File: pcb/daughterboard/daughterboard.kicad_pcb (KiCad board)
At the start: 2 copper layers, 82.5 x 25.4 mm, 0 parts

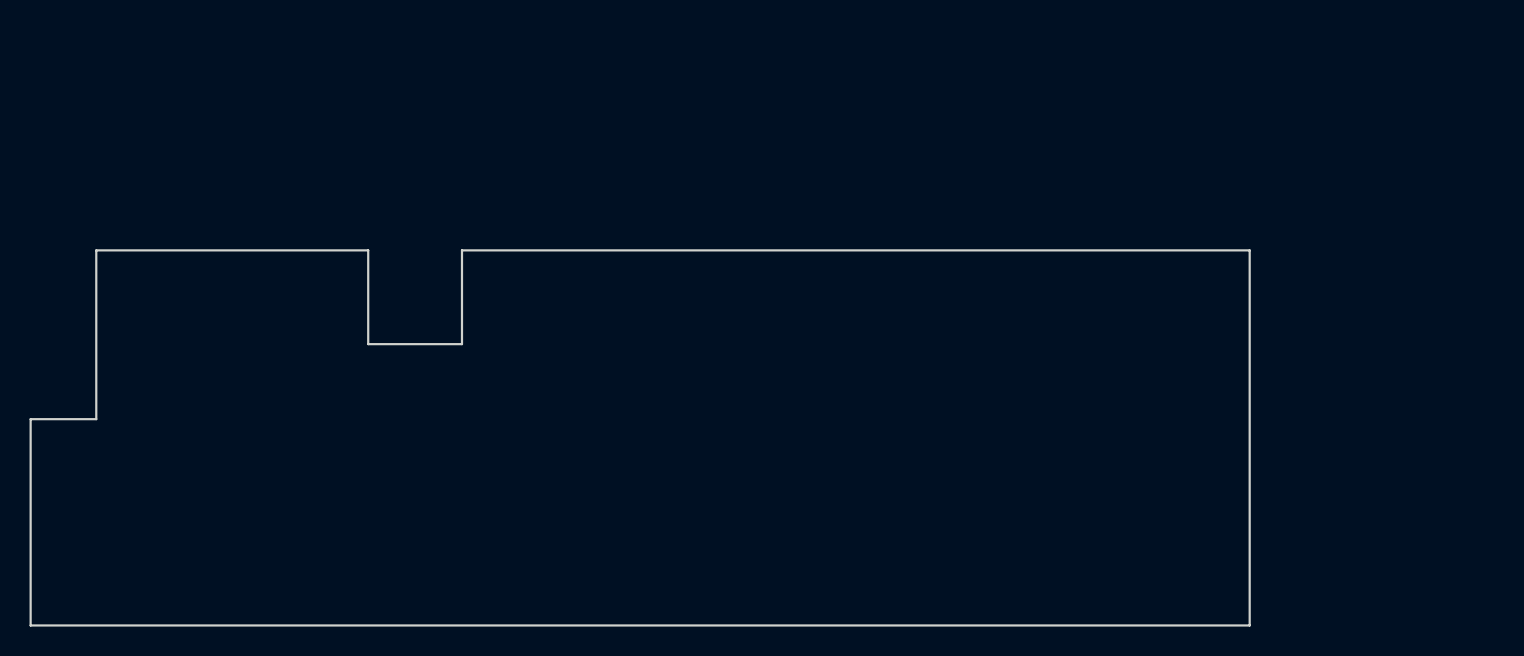
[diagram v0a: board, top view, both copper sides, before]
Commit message: Modified daughterboard board layout
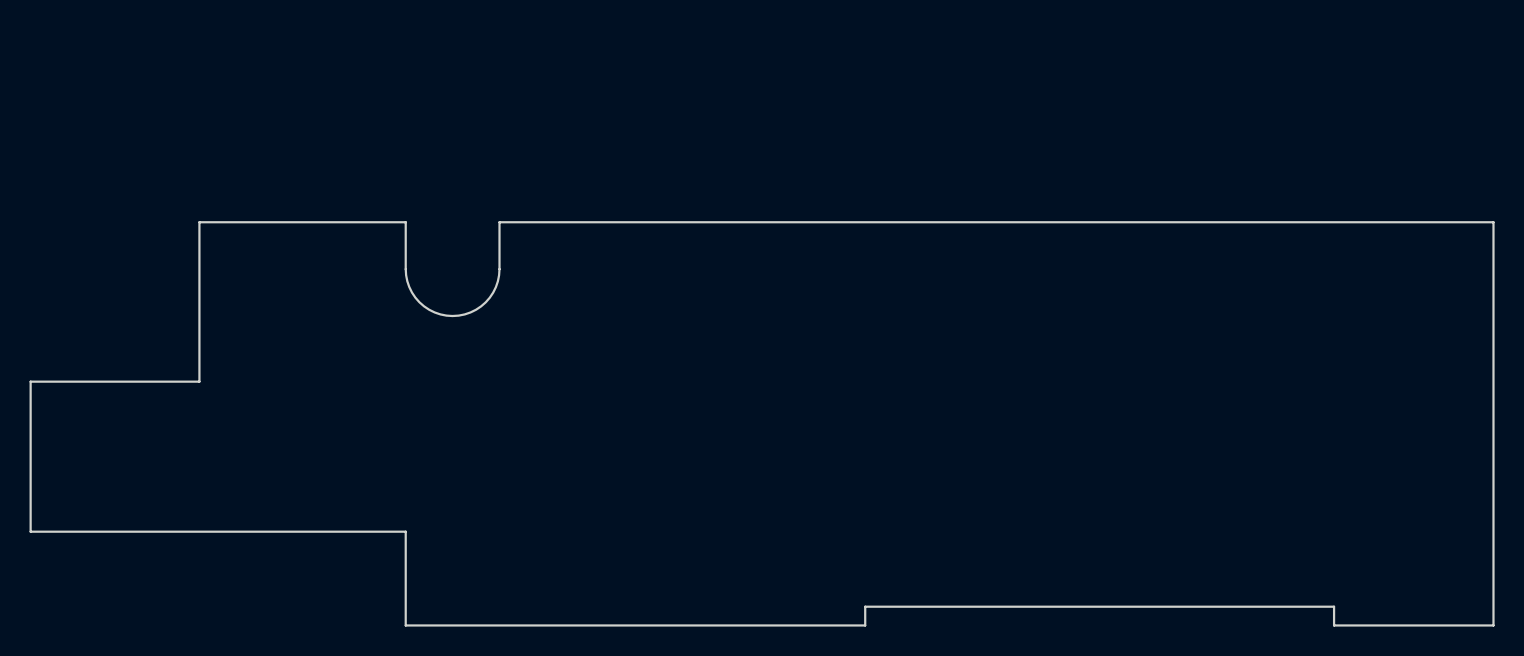
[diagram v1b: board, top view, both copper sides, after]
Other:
- board size 82.5 x 25.4 mm -> 99.1 x 27.3 mm
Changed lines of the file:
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@@
-(kicad_pcb (version 4) (host pcbnew "(2016-03-01 BZR 6238)-product")
+(kicad_pcb (version 4) (host pcbnew "(2016-05-03 BZR 6266)-product")
   (general
-    (links 3)
-    (no_connects 3)
-    (area 120.574999 87.18 177.875001 114.375001)
+    (links 0)
+    (no_connects 0)
+    (area 120.574999 86.919999 219.785001 114.375001)
     (thickness 1.6)
-    (drawings 10)
+    (drawings 16)
     (tracks 0)
     (zones 0)
@@
     (uvia_dia 0.3)
     (uvia_drill 0.1)
-    (add_net "Net-(J1-Pad1)")
-    (add_net "Net-(J1-Pad2)")
-    (add_net "Net-(J1-Pad3)")
-    (add_net "Net-(J1-Pad4)")
-    (add_net "Net-(J1-Pad5)")
-    (add_net "Net-(J1-Pad6)")
-    (add_net "Net-(J1-Pad7)")
-    (add_net "Net-(J1-Pad8)")
-    (add_net "Net-(J1-PadDC)")
-    (add_net "Net-(J1-PadDT)")
-    (add_net "Net-(J1-PadSH)")
   )
-  (gr_line (start 203.2 114.3) (end 120.65 114.3) (layer Edge.Cuts) (width 0.15))
-  (gr_line (start 203.2 88.9) (end 203.2 114.3) (layer Edge.Cuts) (width 0.15))
-  (gr_line (start 149.86 88.9) (end 203.2 88.9) (layer Edge.Cuts) (width 0.15))
-  (gr_line (start 149.86 95.25) (end 149.86 88.9) (layer Edge.Cuts) (width 0.15))
-  (gr_line (start 143.51 95.25) (end 149.86 95.25) (layer Edge.Cuts) (width 0.15))
-  (gr_line (start 143.51 88.9) (end 143.51 95.25) (layer Edge.Cuts) (width 0.15))
-  (gr_line (start 125.095 88.9) (end 143.51 88.9) (layer Edge.Cuts) (width 0.15))
-  (gr_line (start 125.095 100.33) (end 125.095 88.9) (layer Edge.Cuts) (width 0.15))
-  (gr_line (start 120.65 100.33) (end 125.095 100.33) (layer Edge.Cuts) (width 0.15))
-  (gr_line (start 120.65 114.3) (end 120.65 100.33) (layer Edge.Cuts) (width 0.15))
+  (gr_arc (start 149.225 90.17) (end 152.4 90.17) (angle 180) (layer Edge.Cuts) (width 0.15))
+  (gr_line (start 152.4 86.995) (end 152.4 90.17) (layer Edge.Cuts) (width 0.15))
+  (gr_line (start 146.05 86.995) (end 146.05 90.17) (layer Edge.Cuts) (width 0.15))
+  (gr_line (start 152.4 86.995) (end 219.71 86.995) (layer Edge.Cuts) (width 0.15))
+  (gr_line (start 132.08 86.995) (end 146.05 86.995) (layer Edge.Cuts) (width 0.15))
+  (gr_line (start 132.08 97.79) (end 132.08 86.995) (layer Edge.Cuts) (width 0.15))
+  (gr_line (start 120.65 97.79) (end 132.08 97.79) (layer Edge.Cuts) (width 0.15))
+  (gr_line (start 120.65 107.95) (end 120.65 97.79) (layer Edge.Cuts) (width 0.15))
+  (gr_line (start 219.71 114.3) (end 219.71 86.995) (layer Edge.Cuts) (width 0.15))
+  (gr_line (start 208.915 114.3) (end 219.71 114.3) (layer Edge.Cuts) (width 0.15))
+  (gr_line (start 208.915 113.03) (end 208.915 114.3) (layer Edge.Cuts) (width 0.15))
+  (gr_line (start 177.165 113.03) (end 208.915 113.03) (layer Edge.Cuts) (width 0.15))
+  (gr_line (start 177.165 114.3) (end 177.165 113.03) (layer Edge.Cuts) (width 0.15))
+  (gr_line (start 146.05 114.3) (end 177.165 114.3) (layer Edge.Cuts) (width 0.15))
+  (gr_line (start 146.05 107.95) (end 146.05 114.3) (layer Edge.Cuts) (width 0.15))
+  (gr_line (start 120.65 107.95) (end 146.05 107.95) (layer Edge.Cuts) (width 0.15))
 )

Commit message: Revised touch and front panel PCB, Added Motherboard PCB
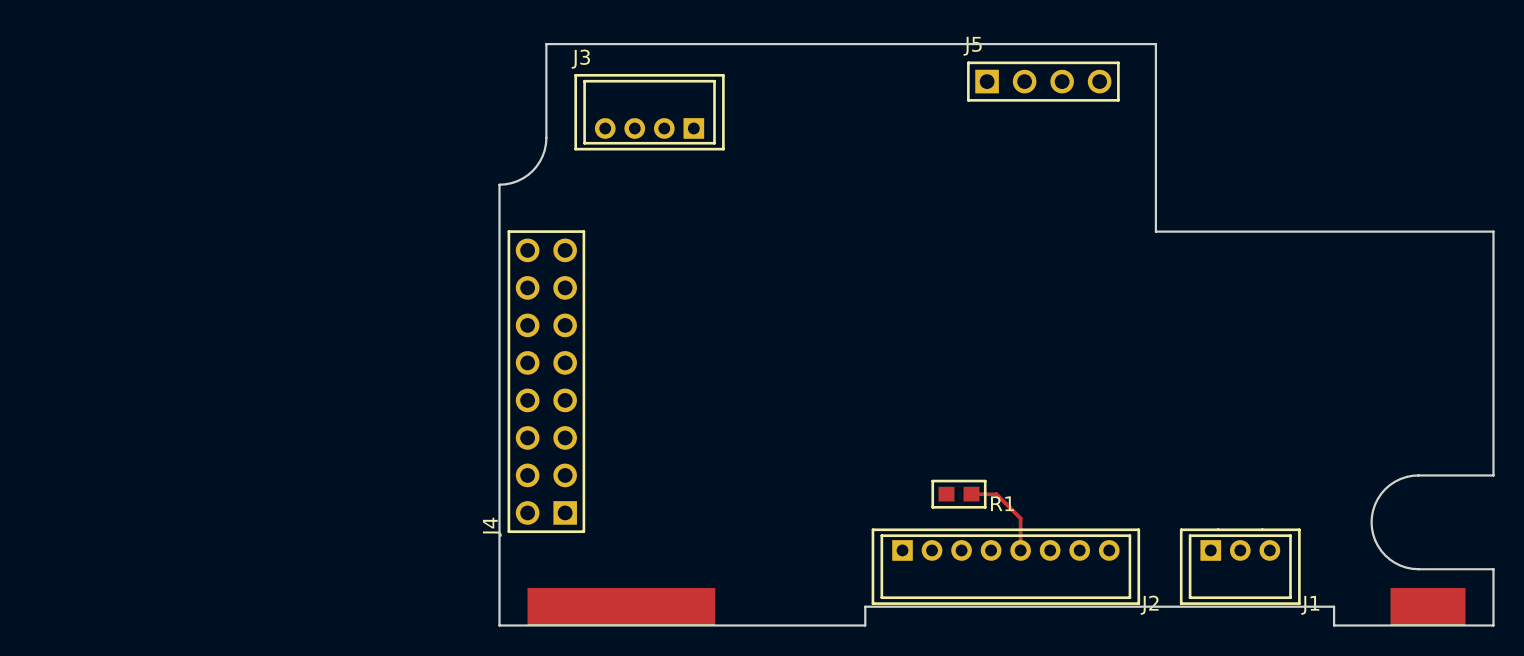
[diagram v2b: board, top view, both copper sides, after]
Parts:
- added H1: HEADER-1x01, conn-wire-pads:SolderPad-100x500, F.Cu at (160.7, 113.0)
- added H2: HEADER-1x01, conn-wire-pads:SolderPad-100x200, F.Cu at (215.3, 113.0)
- added J1: LAMP, conn-header:DF3A-3P-2DSA, F.Cu at (202.6, 109.2)
- added J2: DISPLAY, conn-header:DF3A-8P-2DSA, F.Cu at (186.7, 109.2)
- added J3: SPKR, conn-header:DF3A-4P-2DSA, F.Cu at (162.6, 80.6)
- added J4: MB I/O, conn-header:HDR-M-2x08, F.Cu at (155.6, 97.8)
- added J5: PWR, conn-header:HDR-M-1x04, F.Cu at (189.2, 77.5)
- added R1: 300, smt:R-0603, F.Cu at (183.5, 105.4)
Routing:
- net Net-(J2-Pad5): track 0.00 -> 6.18 mm
- added copper zone on POWER, net +5V
- added copper zone on GND, net GND
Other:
- board size 99.1 x 27.3 mm -> 67.3 x 39.4 mm
- copper layers 2 -> 4

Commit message: Updated PCB design
+ Completed daughterboard PCB layout.
* Corrected soldermask clerance on front panel pcb.
- Removed input resistor on DIN for RGB lamp board.
* Modified PCB layout for PSU board.
* Updated gerber files.
* Updated schematics pdf, BOM.
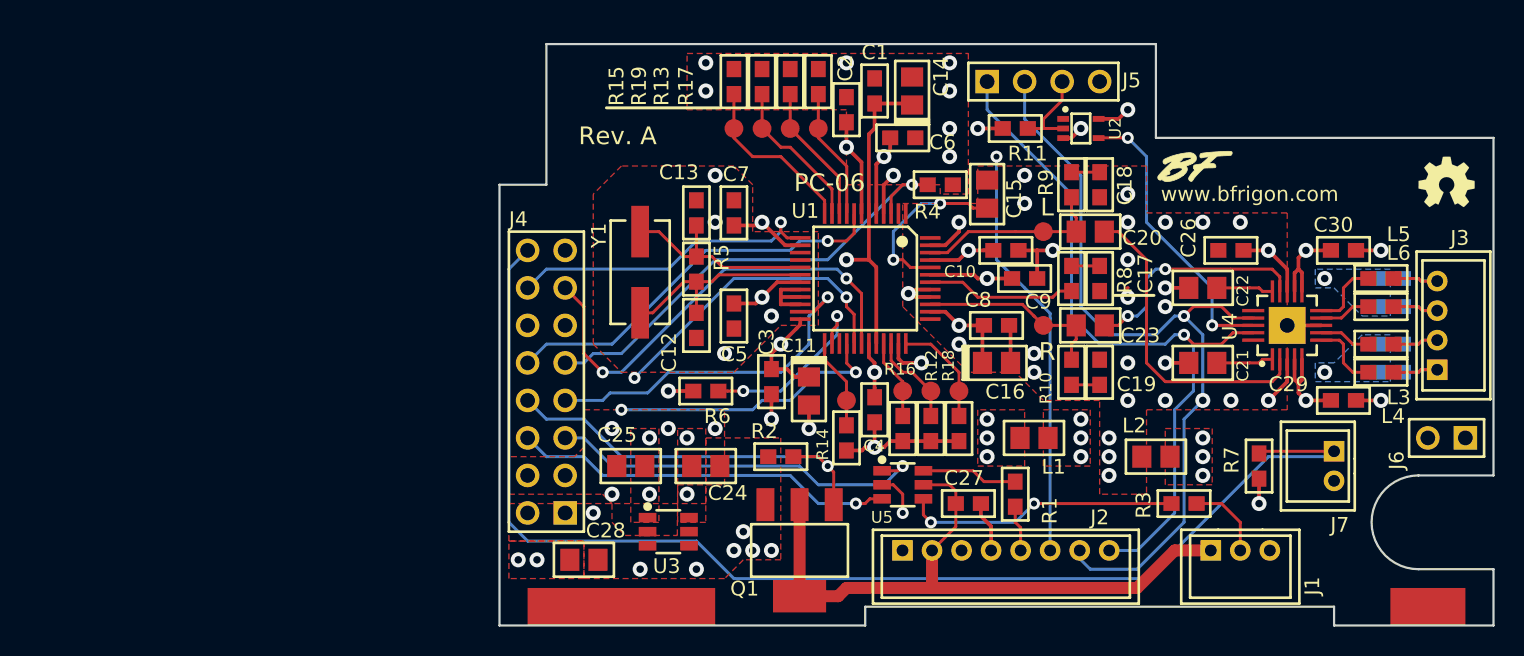
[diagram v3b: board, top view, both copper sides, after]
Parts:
- added C1: 100nF, smt:C-0603, F.Cu at (177.8, 78.1)
- added C10: 100nF, smt:C-0603, F.Cu at (186.7, 88.9)
- added C11: 10uF 6V3, smt:CPL-0805, F.Cu at (173.4, 98.4)
- added C12: 20pF, smt:C-0603, F.Cu at (165.7, 94.0)
- added C13: 20pF, smt:C-0603, F.Cu at (165.7, 86.4)
- added C14: 10uF 6V3, smt:CPL-0805, F.Cu at (180.3, 78.1)
- added C15: 1uF, smt:C-0805, F.Cu at (185.4, 85.1)
- added C16: 10uF 6V3, smt:CPL-0805, F.Cu at (186.1, 96.5)
- added C17: 47nF, smt:C-0603, F.Cu at (193.0, 90.8)
- added C18: 10nF, smt:C-0603, F.Cu at (193.0, 84.5)
- added C19: 10nF, smt:C-0603, F.Cu at (193.0, 97.2)
- added C2: 100nF, smt:C-0603, F.Cu at (175.9, 79.4)
- added C20: 1uF, smt:C-0805, F.Cu at (192.4, 87.6)
- added C21: 1uF, smt:C-0805, F.Cu at (200.0, 96.5)
- added C22: 1uF, smt:C-0805, F.Cu at (200.0, 91.4)
- added C23: 1uF, smt:C-0805, F.Cu at (192.4, 94.0)
- added C24: 10uF, smt:C-0805, F.Cu at (166.4, 103.5)
- added C25: 10uF, smt:C-0805, F.Cu at (161.3, 103.5)
- added C26: 100nF, smt:C-0603, F.Cu at (201.9, 88.9)
- added C27: 100nF, smt:C-0603, F.Cu at (184.2, 106.0)
- added C28: 10uF, smt:C-0805, F.Cu at (158.1, 109.9)
- added C29: 100nF, smt:C-0603, F.Cu at (209.6, 99.1)
- added C3: 100nF, smt:C-0603, F.Cu at (170.8, 97.8)
- added C30: 100nF, smt:C-0603, F.Cu at (209.6, 88.9)
- added C31: 1nF, smt:C-0603, B.Cu at (212.7, 97.2)
- added C32: 1nF, smt:C-0603, B.Cu at (212.7, 90.8)
- added C33: 1nF, smt:C-0603, B.Cu at (212.7, 95.2)
- added C34: 1nF, smt:C-0603, B.Cu at (212.7, 92.7)
- added C4: 100nF, smt:C-0603, F.Cu at (177.8, 99.7)
- added C5: 100nF, smt:C-0603, F.Cu at (168.3, 93.3)
- added C6: 100nF, smt:C-0603, F.Cu at (179.7, 81.3)
- added C7: 100nF, smt:C-0603, F.Cu at (168.3, 86.4)
- added C8: 100nF, smt:C-0603, F.Cu at (186.1, 94.0)
- added C9: 100nF, smt:C-0603, F.Cu at (188.0, 90.8)
- added J6: DB-C, conn-header:HDR-M-1x02, F.Cu at (216.5, 101.6)
- added J7: ALARM SW, conn-header:DF3A-2P-2DSA, F.Cu at (208.9, 103.5)
- added L1: 2508053007Y0, smt:FER-0805, F.Cu at (188.6, 101.6)
- added L2: 2508053007Y0, smt:FER-0805, F.Cu at (196.8, 102.9)
- added L3: MPZ1608S221A, smt:FER-0603, F.Cu at (212.1, 95.2)
- added L4: MPZ1608S221A, smt:FER-0603, F.Cu at (212.1, 97.2)
- added L5: MPZ1608S221A, smt:FER-0603, F.Cu at (212.1, 90.8)
- added L6: MPZ1608S221A, smt:FER-0603, F.Cu at (212.1, 92.7)
- added Q1: NTF6P02, smt-sot:SOT-223, F.Cu at (172.7, 109.2)
- added R10: 20, smt:R-0603, F.Cu at (191.1, 97.2)
- added R11: 10k, smt:R-0603, F.Cu at (187.3, 80.6)
- added R12: 100k, smt:R-0603, F.Cu at (181.6, 101.0)
- added R13: 100k, smt:R-0603, F.Cu at (172.1, 77.5)
- added R14: 100k, smt:R-0603, F.Cu at (175.9, 101.6)
- added R15: 100k, smt:R-0603, F.Cu at (168.3, 77.5)
- added R16: 100k, smt:R-0603, F.Cu at (179.7, 101.0)
- added R17: 100k, smt:R-0603, F.Cu at (174.0, 77.5)
- added R18: 100k, smt:R-0603, F.Cu at (183.5, 101.0)
- added R19: 100k, smt:R-0603, F.Cu at (170.2, 77.5)
- added R2: 10k, smt:R-0603, F.Cu at (171.4, 102.9)
- added R3: 470, smt:R-0603, F.Cu at (198.8, 106.0)
- added R4: 100k, smt:R-0603, F.Cu at (182.2, 84.5)
- added R5: 1M, smt:R-0603, F.Cu at (165.7, 90.2)
- added R6: 100k, smt:R-0603, F.Cu at (166.4, 98.4)
- added R7: 10k, smt:R-0603, F.Cu at (203.8, 103.5)
- added R8: 10, smt:R-0603, F.Cu at (191.1, 90.8)
- added R9: 20, smt:R-0603, F.Cu at (191.1, 84.5)
- added REF**: VAL**, symbols:SIGNATURE_SILK, F.Cu at (199.4, 83.2)
- added REF**: VAL**, symbols:LOGO-OSHW-150, F.Cu at (216.5, 84.5)
- added TP1: TEST-POINT, conn-wire-pads:TEST-POINT-50, F.Cu at (179.7, 98.4)
- added TP10: TEST-POINT, conn-wire-pads:TEST-POINT-50, F.Cu at (189.2, 94.0)
- added TP2: TEST-POINT, conn-wire-pads:TEST-POINT-50, F.Cu at (181.6, 98.4)
- added TP3: TEST-POINT, conn-wire-pads:TEST-POINT-50, F.Cu at (174.0, 80.6)
- added TP4: TEST-POINT, conn-wire-pads:TEST-POINT-50, F.Cu at (172.1, 80.6)
- added TP5: TEST-POINT, conn-wire-pads:TEST-POINT-50, F.Cu at (183.5, 98.4)
- added TP6: TEST-POINT, conn-wire-pads:TEST-POINT-50, F.Cu at (175.9, 99.1)
- added TP7: TEST-POINT, conn-wire-pads:TEST-POINT-50, F.Cu at (170.2, 80.6)
- added TP8: TEST-POINT, conn-wire-pads:TEST-POINT-50, F.Cu at (168.3, 80.6)
- added TP9: TEST-POINT, conn-wire-pads:TEST-POINT-50, F.Cu at (189.2, 87.6)
- added U1: VS1053B, smt-qfp:QFP-7-48, F.Cu at (177.2, 90.8)
- added U2: 74AHC1G04SE-7, smt-sot:SOT-353, F.Cu at (191.8, 80.6)
- added U3: AP7312-1833W6, smt-sot:SOT23-6, F.Cu at (163.8, 108.0)
- added U4: TPA2016D2, smt-qfn:QFN20-EP-4x4, F.Cu at (205.7, 94.0)
- added U5: SN74LVC2G34DBV, smt-sot:SOT23-6, F.Cu at (179.7, 104.8)
- added Y1: 12.288 MHz, crystals:smt-CSM-3X-7x4mm, F.Cu at (161.9, 90.4)
- H1: value HEADER-1x01 -> Solder pad 2
- H2: value HEADER-1x01 -> Solder Pad 2
- J4: value MB I/O -> DB-A
- J5: value PWR -> DB-B
- R1: value 300 -> 470
- moved J3 55.0 mm to (215.9, 94.0), turned to 270 degrees
- moved R1 3.81 mm to (187.3, 105.4), turned to 270 degrees
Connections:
- J1 pad 1: +5V -> /PIX_VCC
- J1 pad 2: /LED1 -> Net-(J1-Pad2)
- J2 pad 2: +5V -> /PIX_VCC
- J2 pad 6: /K_CHG -> /KCHG
- J2 pad 7: /SCL_5V -> /SCL
- J2 pad 8: /SDA_5V -> /SDA
- J3 pad 1: Net-(J3-Pad1) -> /OUT_L-
- J3 pad 2: Net-(J3-Pad2) -> /OUT_L+
- J3 pad 3: Net-(J3-Pad3) -> /OUT_R+
- J3 pad 4: Net-(J3-Pad4) -> /OUT_R-
- J4 pad 1: /MISO -> +5V
- J4 pad 10: /LED0 -> /DREQ
- J4 pad 11: /LED1 -> /CMOSI_3V3
- J4 pad 12: /CD_RST -> /SCLK_3V3
- J4 pad 13: /A_SHDN -> /MISO
- J4 pad 14: /LED_SHDN -> /XDCS_3V3
- J4 pad 15: Net-(J4-Pad15) -> +3V3
- J4 pad 16: /RESET -> /ALRM_SW
- J4 pad 2: /MOSI -> +5V
- J4 pad 3: /SCLK -> GND
- J4 pad 4: /CD_XDCS -> GND
- J4 pad 5: /DREQ -> /PIX_CLK
- J4 pad 6: /CD_CS -> /PIX_LAMP
- J4 pad 7: /SDA_5V -> /CCS_3V3
- J4 pad 8: /SCL_5V -> /PIX_SHDN
- J4 pad 9: /K_CHG -> /CRST_3V3
- J5 pad 1: +5V -> /SDA
- J5 pad 2: +5V -> /SCL
- J5 pad 3: GND -> /A_SHDN
- J5 pad 4: GND -> /KCHG
- R1 pad 1: Net-(J2-Pad5) -> Net-(R1-Pad1)
- R1 pad 2: /LED0 -> Net-(J2-Pad5)
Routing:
- net /ALRM_SW: track 0.00 -> 85.0 mm
- net /SCL: track 0.00 -> 54.6 mm, vias 0 -> 2
- net +5V: track 0.00 -> 53.7 mm, vias 0 -> 12
- net /SDA: track 0.00 -> 50.5 mm, vias 0 -> 1
- net /PIX_VCC: track 0.00 -> 46.1 mm
- net /KCHG: track 0.00 -> 39.5 mm, vias 0 -> 1
- net GND: track 0.00 -> 36.9 mm, vias 0 -> 29
- net +3V3: track 0.00 -> 32.7 mm, vias 0 -> 9
- net /CRST_3V3: track 0.00 -> 32.5 mm, vias 0 -> 1
- net /MISO: track 0.00 -> 31.3 mm, vias 0 -> 2
- net /SCLK_3V3: track 0.00 -> 31.0 mm, vias 0 -> 2
- net /CMOSI_3V3: track 0.00 -> 28.7 mm, vias 0 -> 2
- net /PIX_SHDN: track 0.00 -> 27.5 mm, vias 0 -> 1
- net /DREQ: track 0.00 -> 27.1 mm, vias 0 -> 1
- net /PIX_CLK: track 0.00 -> 26.2 mm, vias 0 -> 1
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- added copper zone on F.Cu, net +1V8
- added copper zone on POWER, net +1V8
- added copper zone on F.Cu, net +3V3
- added copper zone on POWER, net +3V3
- added copper zone on F.Cu, net +5V
- added copper zone on B.Cu, net AGND
- added copper zone on F.Cu, net AGND
- added copper zone on GND, net AGND
- added copper zone on F.Cu, net AVDD
- added copper zone on POWER, net AVDD
- added copper zone on F.Cu, net GND
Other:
- outline, holes or cut-outs redrawn
- net class Default: clearance 0.2 -> 0.2032; trace_width 0.25 -> 0.2032; via_dia 0.6 -> 0.8128; via_drill 0.4 -> 0.4064
- net class PIX_VCC added: clearance 0.4064, trace_width 0.8128, via_dia 1.27, via_drill 0.508
- net class Power added: clearance 0.2032, trace_width 0.254, via_dia 1.016, via_drill 0.508
- rule trace_clearance: 0.2 -> 0.2032
- rule trace_min: 0.2 -> 0.2032
- rule via_min_drill: 0.3 -> 0.4064
- rule via_min_size: 0.4 -> 0.6096
- board text added: "L"
- board text added: "PC-06"
- board text added: "R"
- board text added: "Rev. A"
- board text added: "www.bfrigon.com"

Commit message: Corrected solder mask clearance
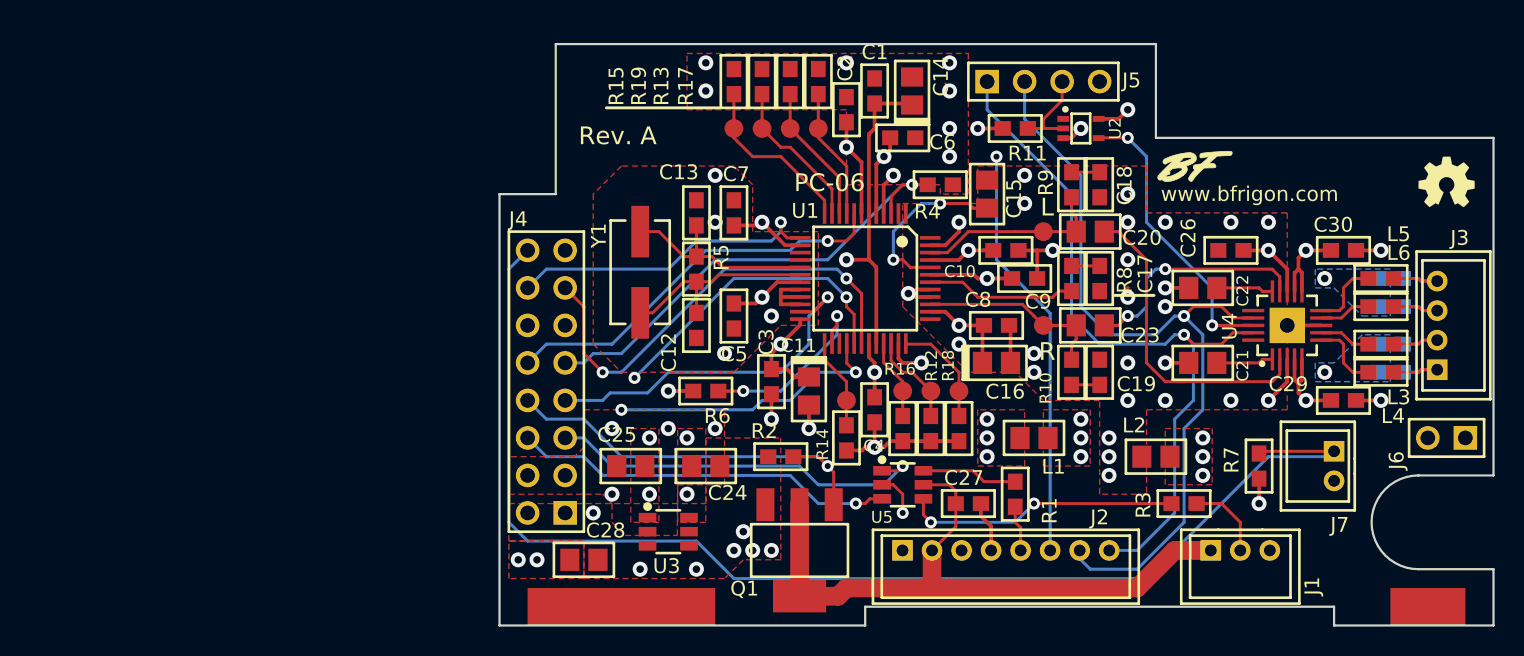
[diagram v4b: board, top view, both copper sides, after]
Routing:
- net +5V: track 53.7 -> 50.9 mm
- net /SCL: vias 2 -> 1
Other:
- outline, holes or cut-outs redrawn
- rule pad_to_mask_clearance: 0.2 -> 0.1016
